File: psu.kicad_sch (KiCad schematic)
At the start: 0 parts

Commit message: feat(psu): Added USB-C power circuit
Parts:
- added C61: 1uF/16V, A_HDJ_Library:C_0402_1005Metric, symbol Device:C_Small
- added D10, D11: ESD9B5.0ST5G, A_HDJ_Library:D_0402_1005Metric, symbol Diode:ESD9B5.0ST5G
- added D12, D13, D14: D_Zener, A_HDJ_Library:D_0402_1005Metric, symbol Device:D_Zener
- added J18: USB_C_Receptacle_USB2.0_16P, symbol Connector:USB_C_Receptacle_USB2.0_16P
- added R36: 10k/1%, A_HDJ_Library:R_0402_1005Metric, symbol Device:R
- added R37: 1k/1%, A_HDJ_Library:R_0402_1005Metric, symbol Device:R
- added R43: 56k/1%, A_HDJ_Library:R_0402_1005Metric, symbol Device:R
- added U?: USB PD等快充协议受电芯片-CH224K-ESSOP10, A_HDJ_Library:ESSOP-10-1EP_3.9x5mm_P1.0mm_EP3.2x2.3, symbol A_HDJ_Library:CH224K
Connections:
- new net: R36.2, U?.8 (VBUS)
- new net: R43.1, U?.9 (CFG1)
- new net: C61.1, R37.2, U?.1 (VDD)
- new net +15V: D12.1 (K), J18.A4 (VBUS), J18.A9 (VBUS), J18.B4 (VBUS), J18.B9 (VBUS), R36.1
- new net CC1: D13.1 (K), J18.A5 (CC1), U?.7 (CC1)
- new net CC2: D14.1 (K), J18.B5 (CC2), U?.6 (CC2)
- new net GND: C61.2, D10.1 (A1), D11.1 (A1), D12.2 (A), D13.2 (A), D14.2 (A), J18.A1 (GND), J18.A12 (GND), J18.B1 (GND), J18.B12 (GND), J18.SH (SHIELD), R37.1, R43.2, U?.0 (GND)
- new net PWR_C_D+: D11.2 (A2), J18.A6 (D+), J18.B6 (D+), U?.4 (DP)
- new net PWR_C_D-: D10.2 (A2), J18.A7 (D-), J18.B7 (D-), U?.5 (DM)
- no-connect marks 0 -> 5
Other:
- note added: "CH224K get DC 15V power from USB-PD adapter"

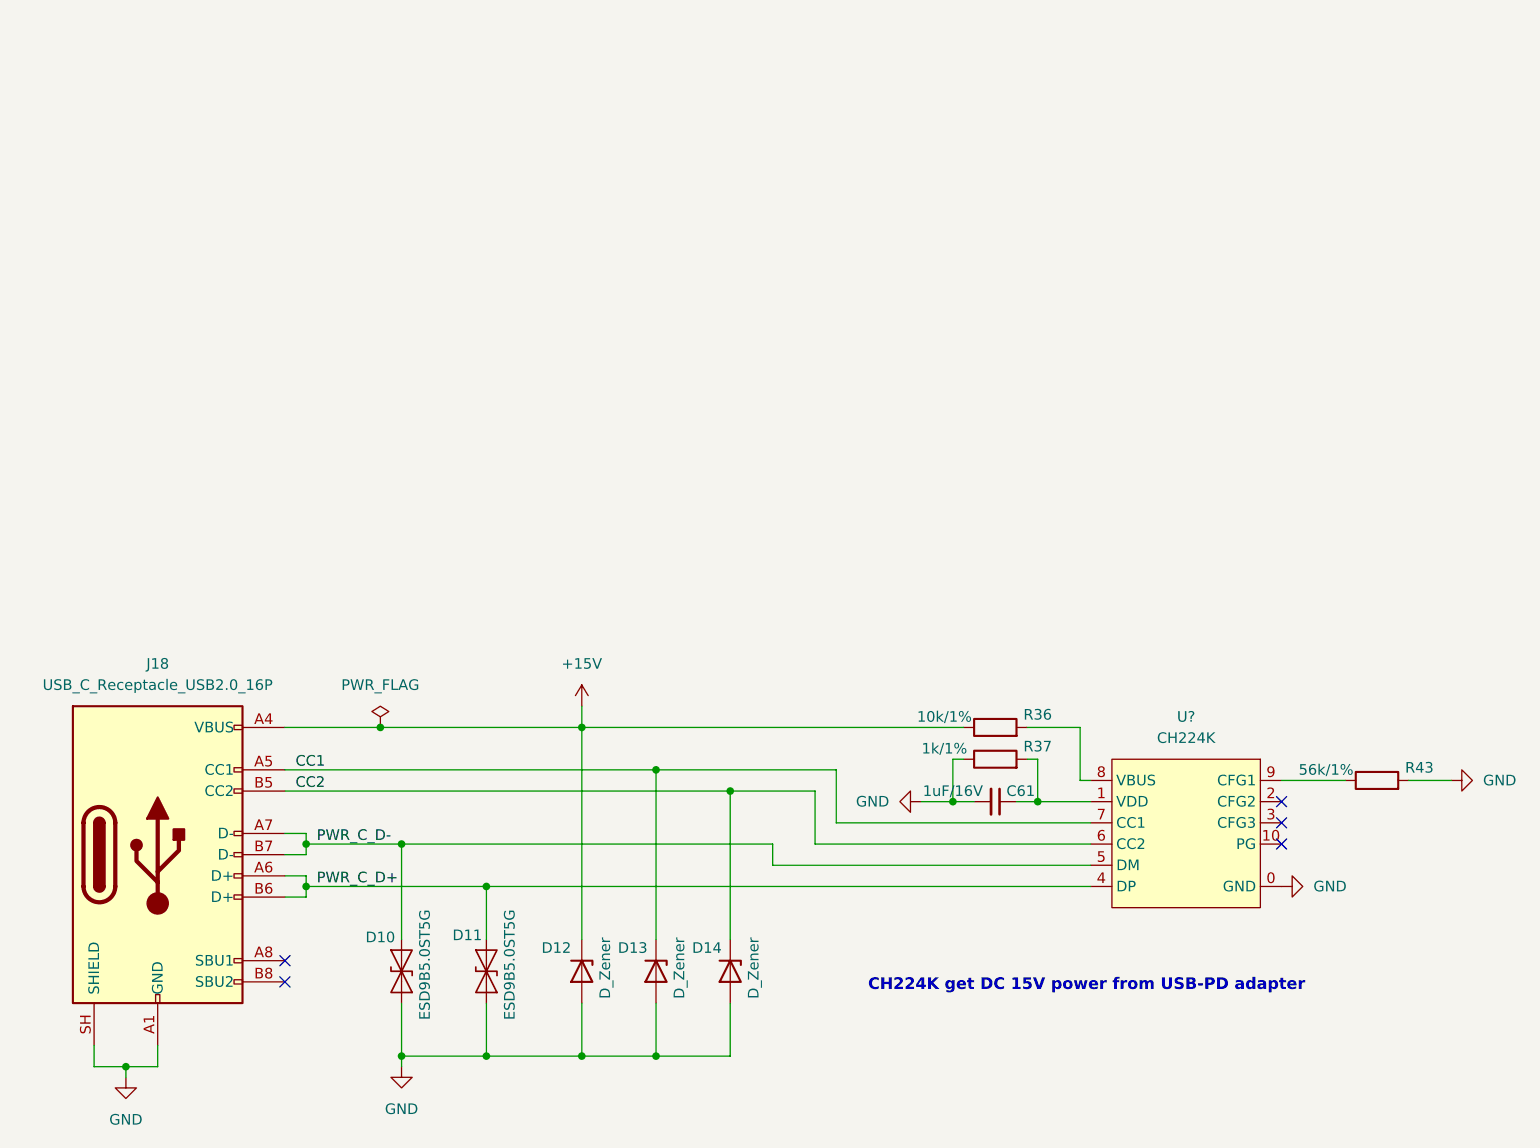
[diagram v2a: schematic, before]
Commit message: feat(psu): Added barrel jack connector circuit
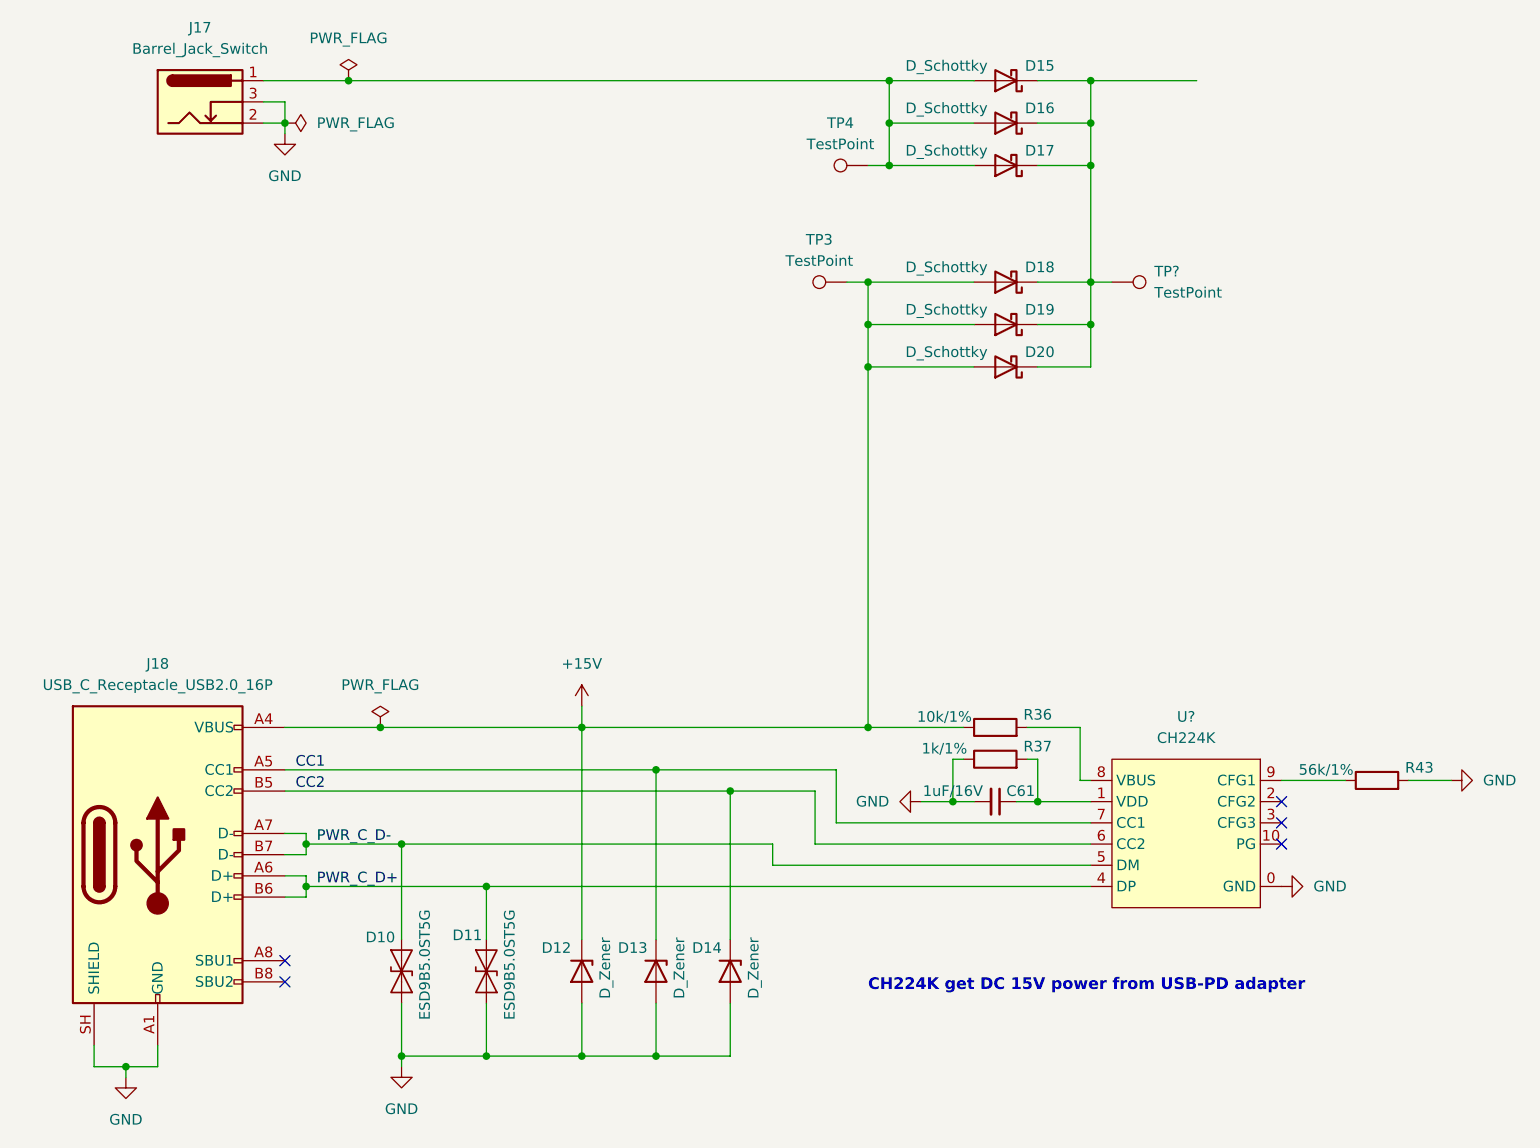
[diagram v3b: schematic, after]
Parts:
- added D15, D16, D17, D18, D19, D20: D_Schottky, A_HDJ_Library:D_SMA, symbol Device:D_Schottky
- added J17: Barrel_Jack_Switch, A_HDJ_Library:DC_Jack_DC007B_30V_10A, symbol Connector:Barrel_Jack_Switch
- added TP3, TP4, TP?: TestPoint, symbol Connector:TestPoint
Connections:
- net +15V: now also D18.2 (A), D19.2 (A), D20.2 (A), TP3.1
- net GND: now also J17.2, J17.3
- new net: D15.1 (K), D16.1 (K), D17.1 (K), D18.1 (K), D19.1 (K), D20.1 (K), TP?.1
- new net: D15.2 (A), D16.2 (A), D17.2 (A), J17.1, TP4.1
